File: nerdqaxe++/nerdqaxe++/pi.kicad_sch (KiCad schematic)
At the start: 22 parts, among them J5 Conn_01x12-Socket, J6 Conn_01x12-Socket, J7 Conn_01x12-Header, J8 Conn_01x12-Header, M1 Fan_4pin, M2 Fan_4pin, U30 T-Display-S3, U32 EMC2302-1, U33 TXU0102-DCU, U37 TMP1075, U38 TMP1075

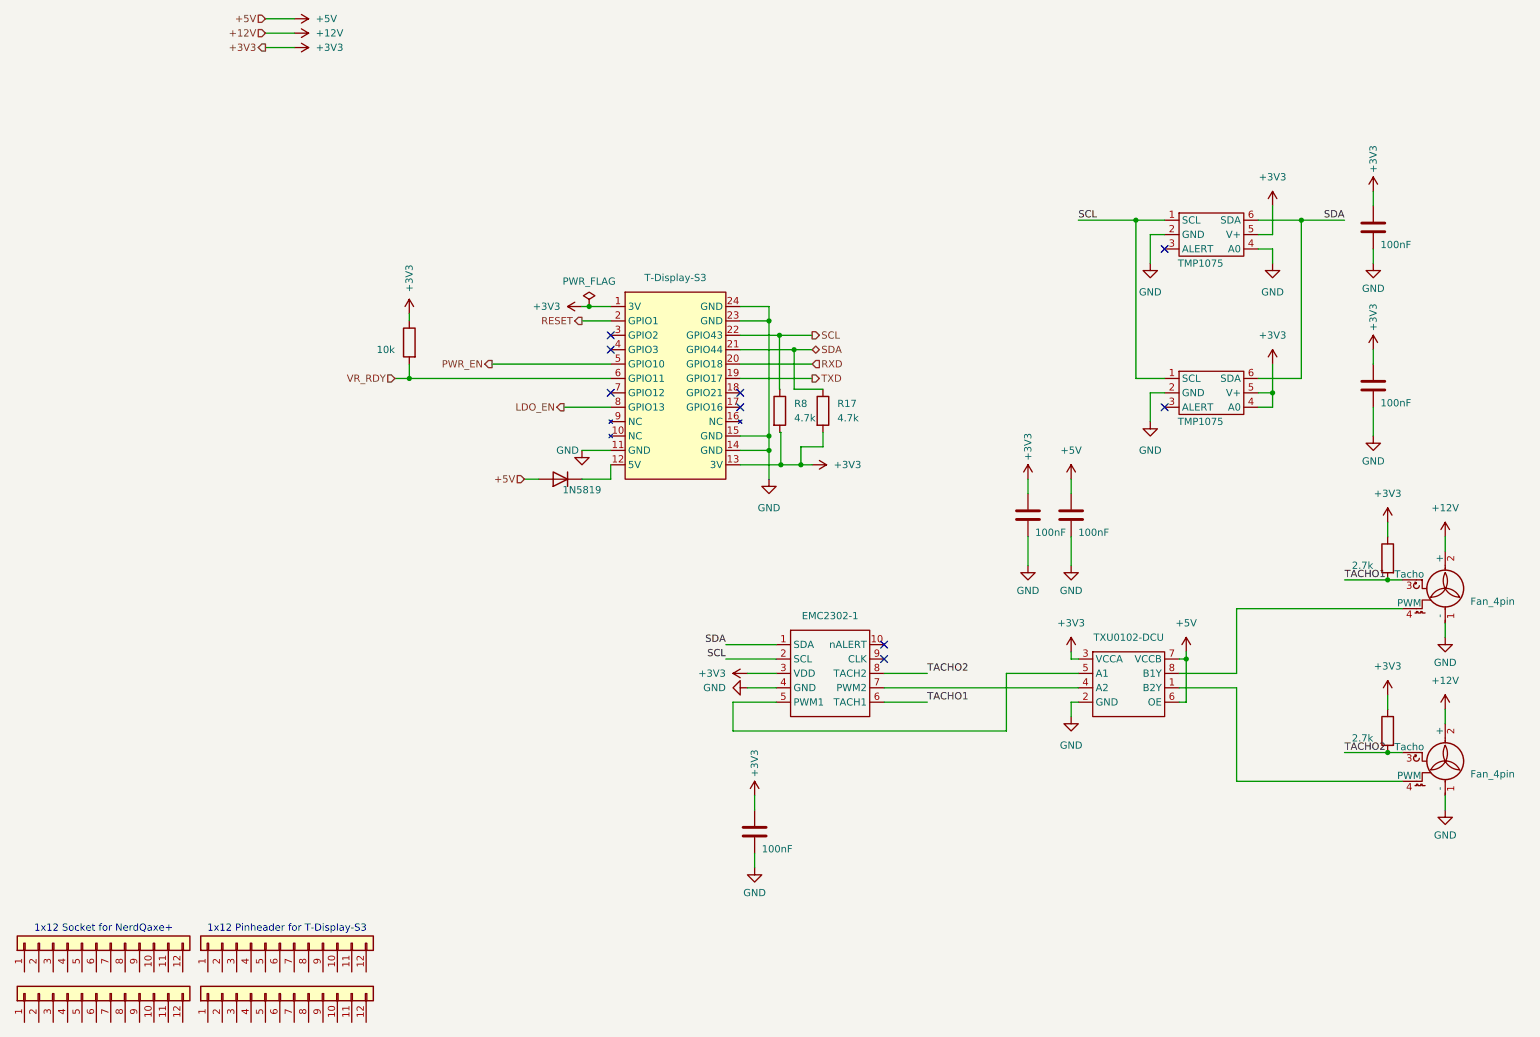
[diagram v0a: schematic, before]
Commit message: Edit on rev 6.1PM
- Moved XT30 connector to the back of the board
- Edited VDD polygon
- Fixed various via placements
- Fixed various tracing
- Updated BM1370 footprint and solder paste stencil
- Updated CSD95472Q5MC footprint and solder paste stencil
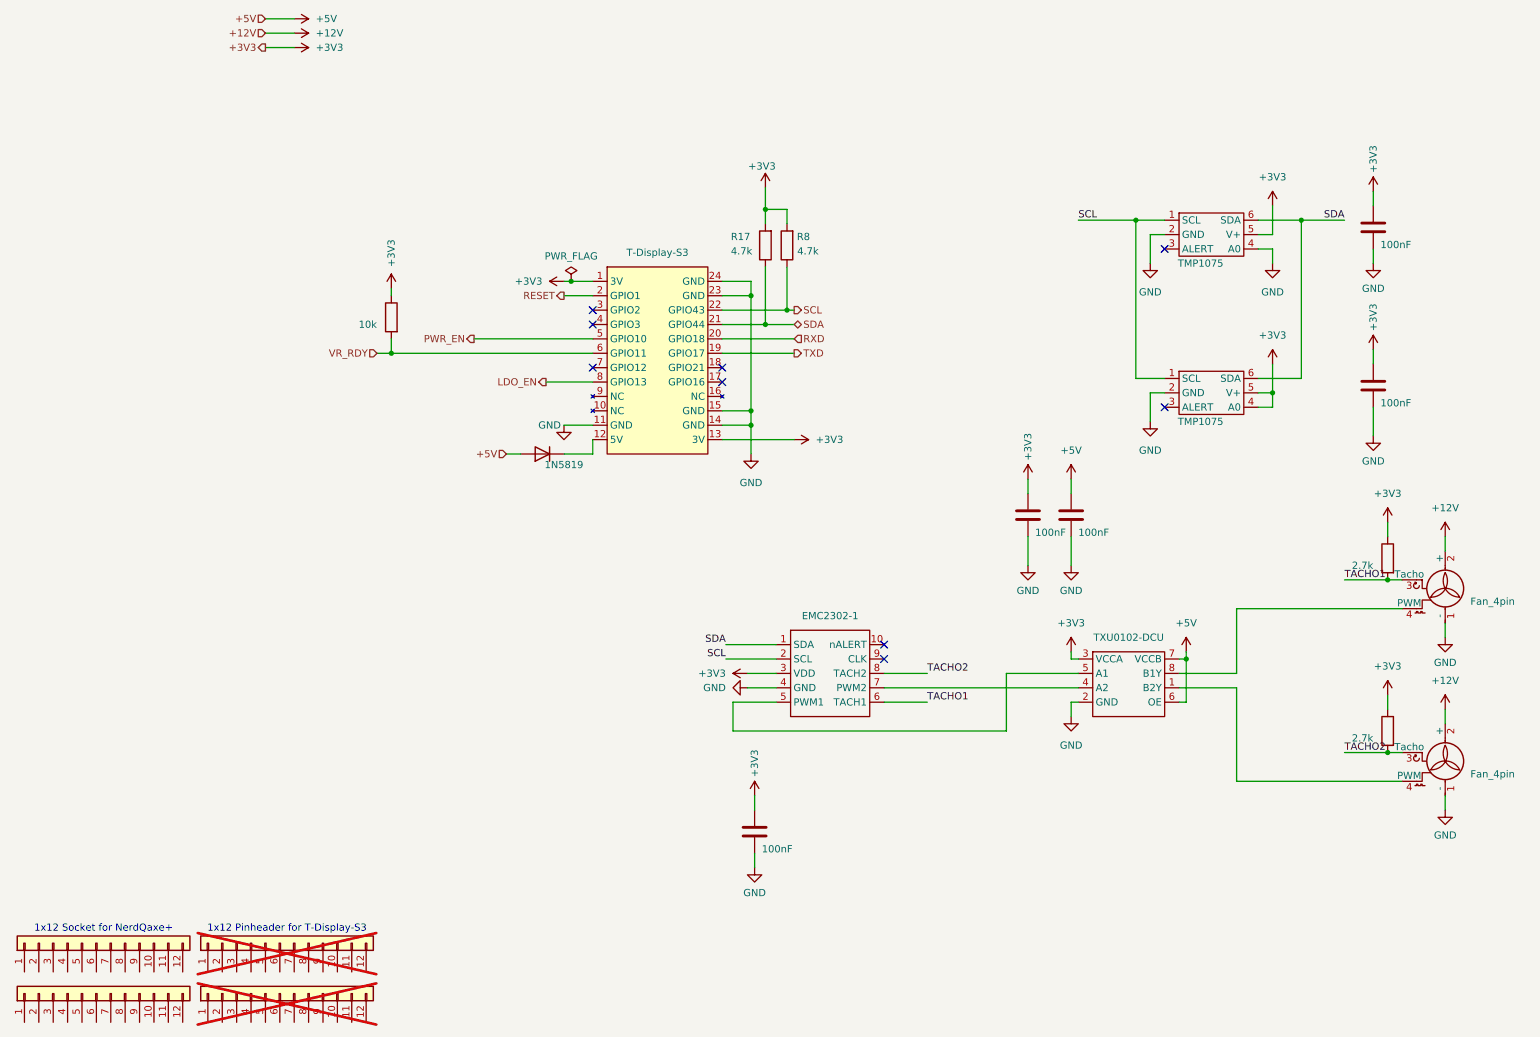
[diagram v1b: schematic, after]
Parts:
- J5, J6: footprint (none) -> Connector_PinSocket_2.54mm:PinSocket_1x12_P2.54mm_Vertical; Manufacturer  (none) -> Würth Elektronik
- J7, J8: now not fitted
- M1, M2: Manufacturer  (none) -> Molex
- R17, R8: LCSC (none) -> C5455562; Manufacturer  (none) -> YAGEO; PARTNO (none) -> RES 4.7K OHM 1% 1/8W 0402
- U30: Manufacturer  (none) -> LILYGO; PARTNO (none) -> T-Display-S3 [H577]
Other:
- moved on the sheet: R17, R8
